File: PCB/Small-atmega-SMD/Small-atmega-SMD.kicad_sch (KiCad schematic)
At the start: 28 parts, among them J1 Daisy port out, J2 ICSP_ISP6, J3 UART, J4 Daisy port in, K1 HYC77-TF09-200, U1 PC817C-S, U2 ATmega328P-AU, U3 SE5218, U4 TXB0104PWR, Y1 Crystal_GND2

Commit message: More OCD
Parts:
- Y1: value Crystal_GND2 -> Resonator_GND2
- renumbered C5 to C2, C2 to C3, C3 to C4, C4 to C5
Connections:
- net RDDATA_in renamed RDDATA
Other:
- note added: "APPLE II INTERFACE"
- note added: "MICROSD CARD HOLDER"
- note added: "MICROSD LEVEL SHIFTER"
- note added: "MICROSD VOLTAGE REGULATOR"
- note added: "MINIMAL "ARDUINO NANO""
- note removed: "MICRO SD CARD HOLDER & CAPACITOR"
- note removed: "VOLTAGE LEVEL TRANSLATOR"
- note removed: "VOLTAGE REGULATOR"
- title: BurgerDisk PCB - Angled DB19 version -> Integrated Small BurgerDisk PCB
- moved on the sheet: C1, C2, C3, C4, C5, C6, C7, C8, D1, D2, D3, J1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

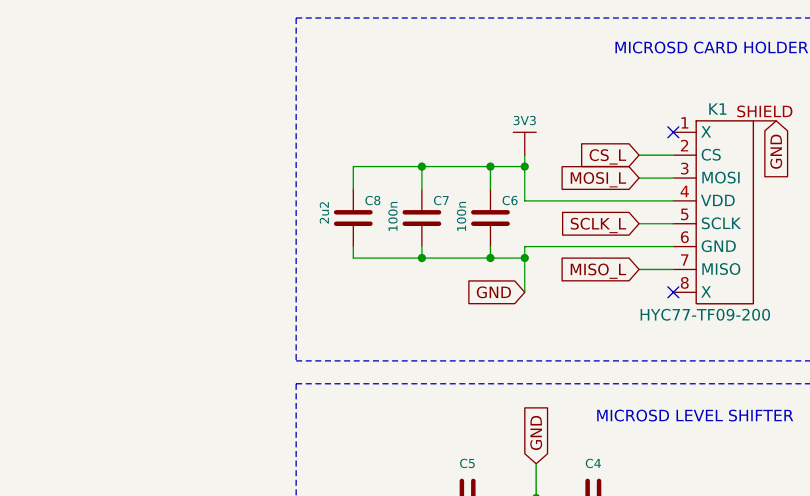
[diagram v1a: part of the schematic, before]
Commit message: Fix microSD caps
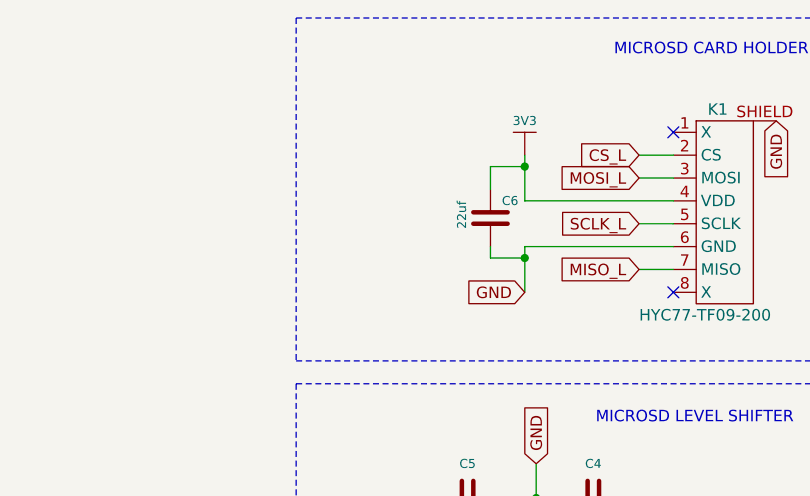
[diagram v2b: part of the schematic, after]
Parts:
- removed C7: 100n, Capacitor_SMD:C_0603_1608Metric, symbol e-radionica.com schematics:0603C
- removed C8: 2u2, Capacitor_SMD:C_0603_1608Metric, symbol e-radionica.com schematics:0603C
- C6: value 100n -> 22uf; footprint Capacitor_SMD:C_0603_1608Metric -> Capacitor_SMD:C_0805_2012Metric; LCSC C1590 -> C45783

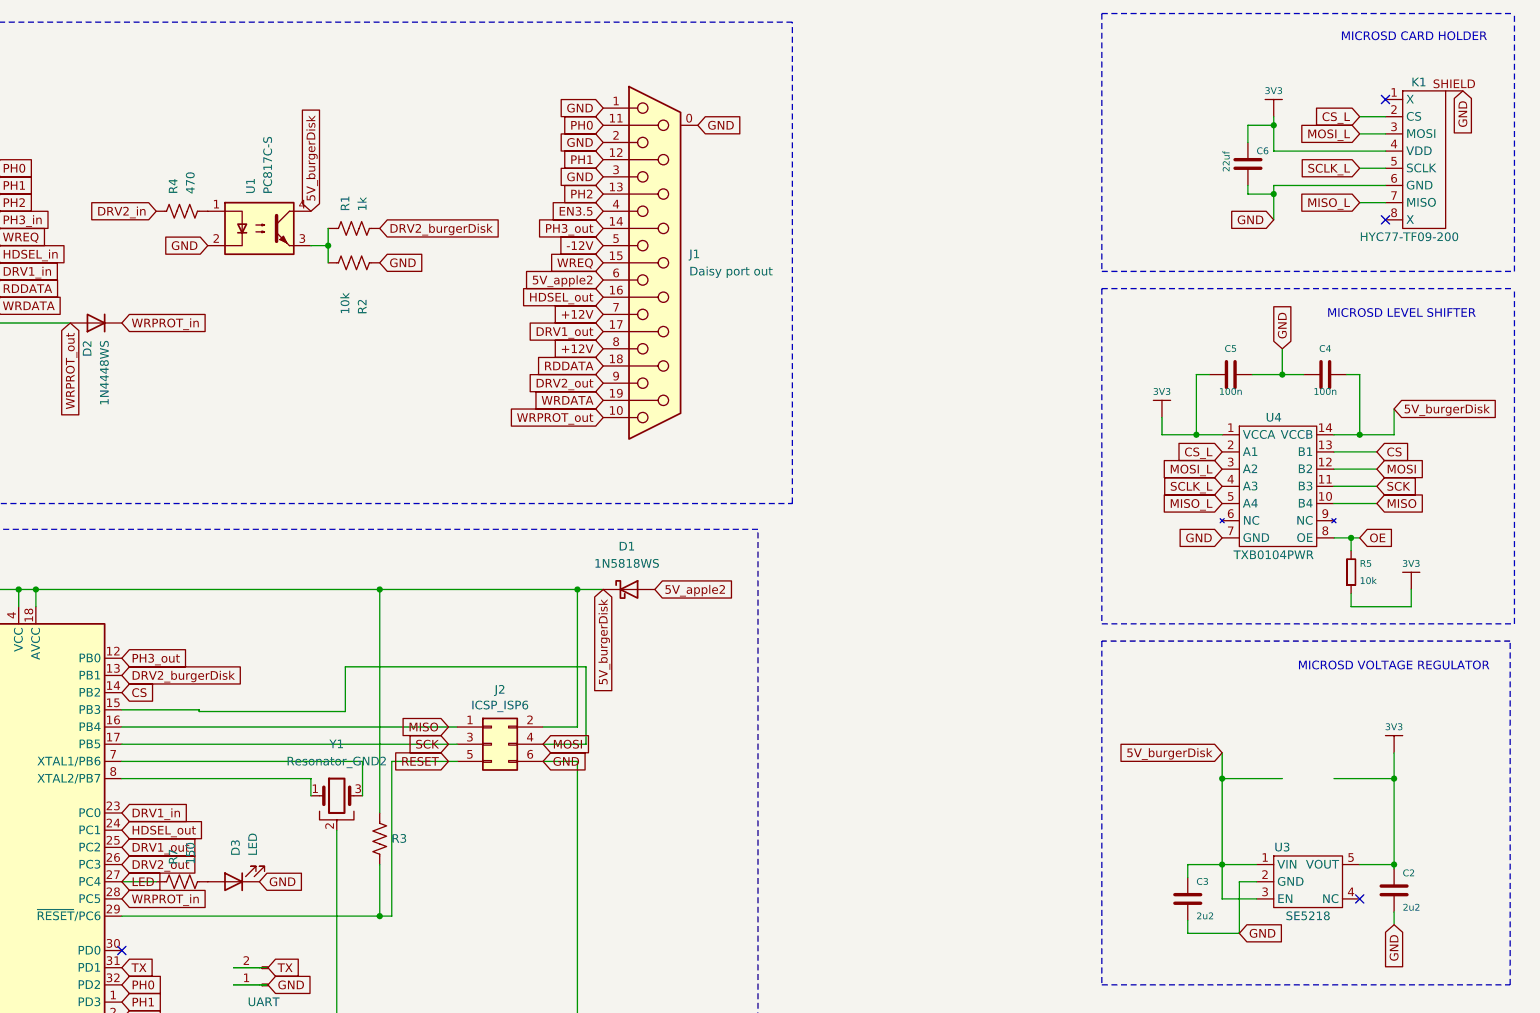
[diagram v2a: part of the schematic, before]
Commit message: Add SD module header, for hackers
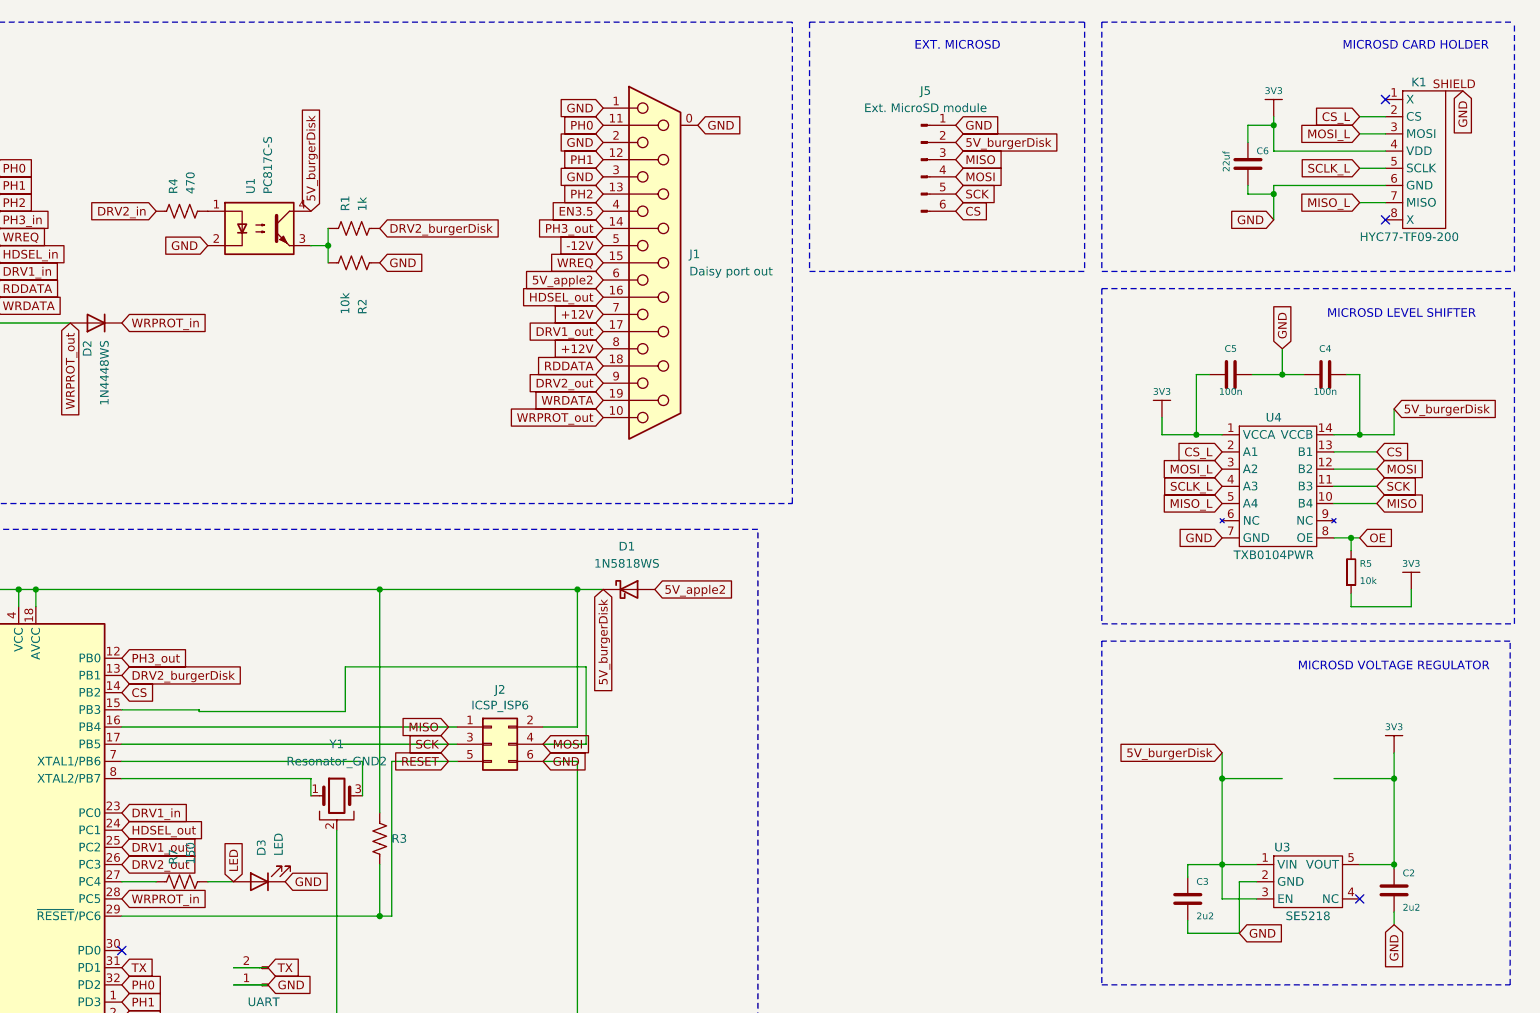
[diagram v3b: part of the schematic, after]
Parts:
- added J5: Ext. MicroSD module, Connector_PinHeader_2.54mm:PinHeader_1x06_P2.54mm_Vertical, symbol Connector:Conn_01x06_Pin
- C1: LCSC C28233 -> C1590
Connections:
- net 5V_burgerDisk: now also J5.2 (Pin_2)
- net CS: now also J5.6 (Pin_6)
- net GND: now also J5.1 (Pin_1)
- net LED: now also D3.2 (A), R7.1; no longer R7.2, U2.27 (PC4)
- net MISO: now also J5.3 (Pin_3)
- net MOSI: now also J5.4 (Pin_4)
- net SCK: now also J5.5 (Pin_5)
- new net: R7.2, U2.27 (PC4)
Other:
- note added: "EXT. MICROSD"
- moved on the sheet: D3

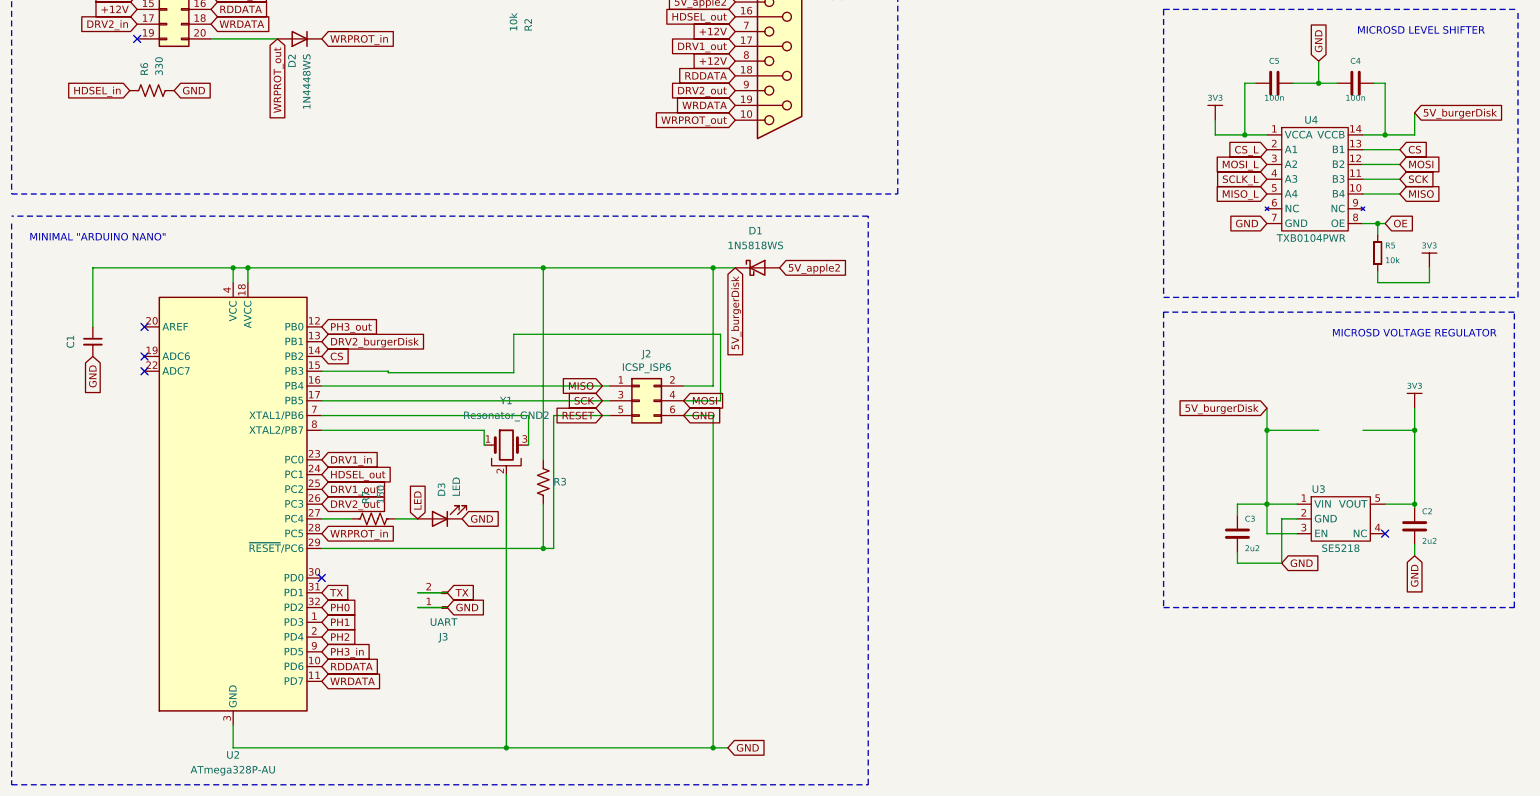
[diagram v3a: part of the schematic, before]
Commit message: Add solder pads for hacking
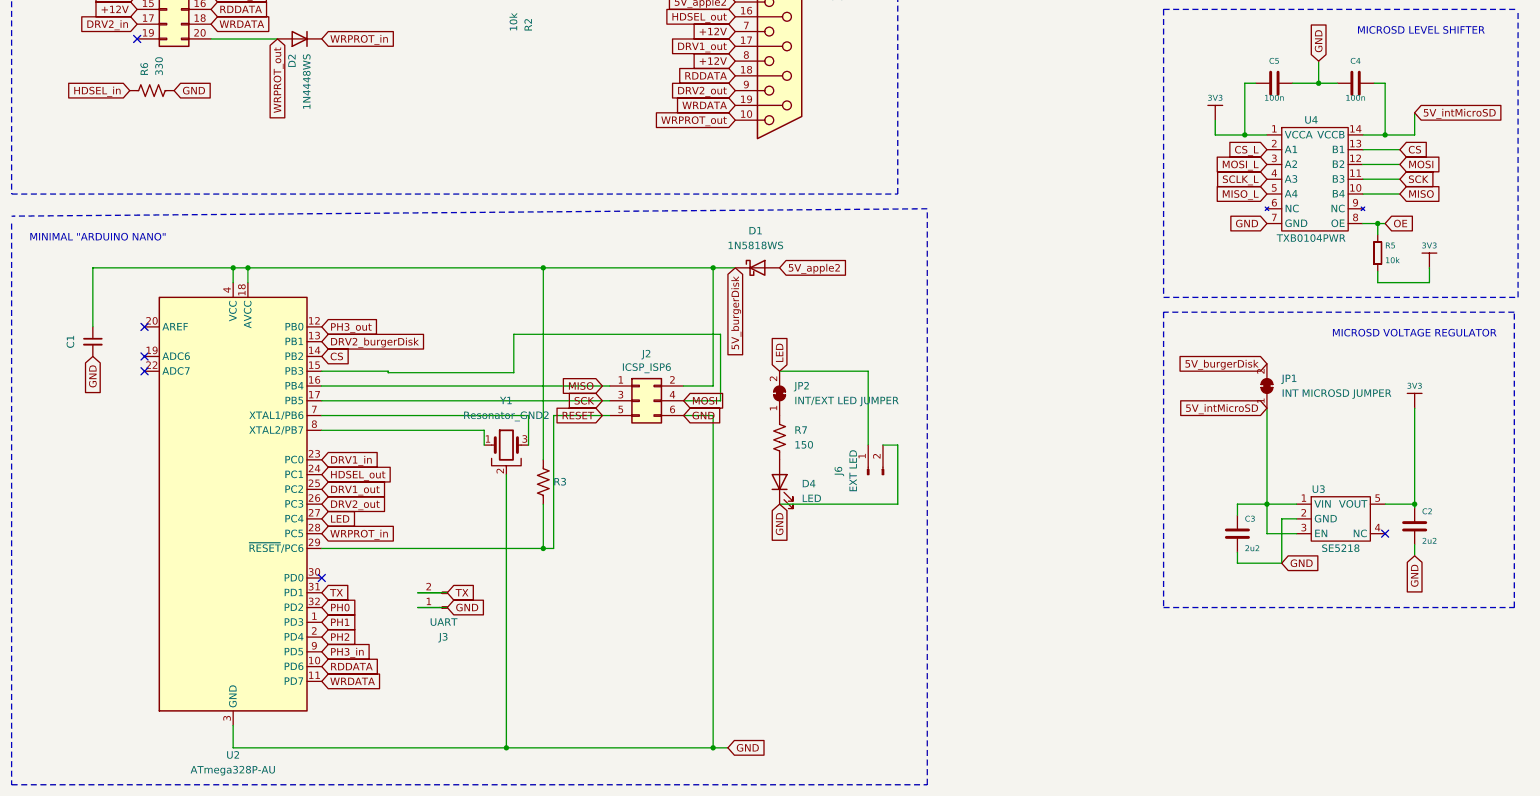
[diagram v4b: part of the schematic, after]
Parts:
- removed D3: LED, LED_THT:LED_D3.0mm, symbol Device:LED
- added D4: LED, LED_THT:LED_D3.0mm, symbol Device:LED
- added J6: EXT LED, Connector_PinHeader_2.54mm:PinHeader_1x02_P2.54mm_Vertical, symbol Connector:Conn_01x02_Pin
- added JP1: INT MICROSD JUMPER, Jumper:SolderJumper-2_P1.3mm_Bridged_Pad1.0x1.5mm, symbol Jumper:SolderJumper_2_Bridged
- added JP2: INT/EXT LED JUMPER, Jumper:SolderJumper-2_P1.3mm_Bridged_Pad1.0x1.5mm, symbol Jumper:SolderJumper_2_Bridged
- C1: value 100nF -> 100n
- J3: LCSC C6273326 -> C32713268
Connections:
- net 5V_burgerDisk: now also JP1.2 (B); no longer C3.2, C4.2, U3.1 (VIN), U3.3 (EN), U4.14 (VCCB)
- net GND: now also D4.1 (K), J6.2 (GND)
- net LED: now also U2.27 (PC4), J6.1 (+5V), JP2.2 (B); no longer R7.1
- net at R7.2: now also JP2.1 (A); no longer U2.27 (PC4)
- new net: D4.2 (A), R7.1
- new net 5V_intMicroSD: C3.2, C4.2, JP1.1 (A), U3.1 (VIN), U3.3 (EN), U4.14 (VCCB)
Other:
- moved on the sheet: R7

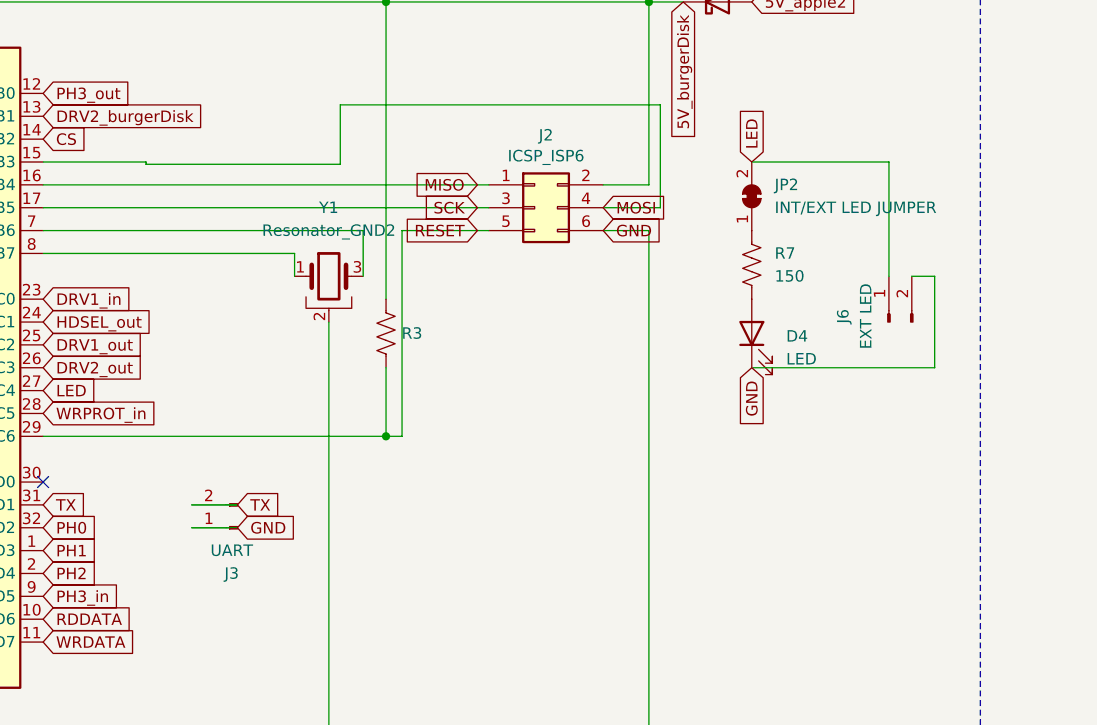
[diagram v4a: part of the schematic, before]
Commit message: Switch some parts to Basic
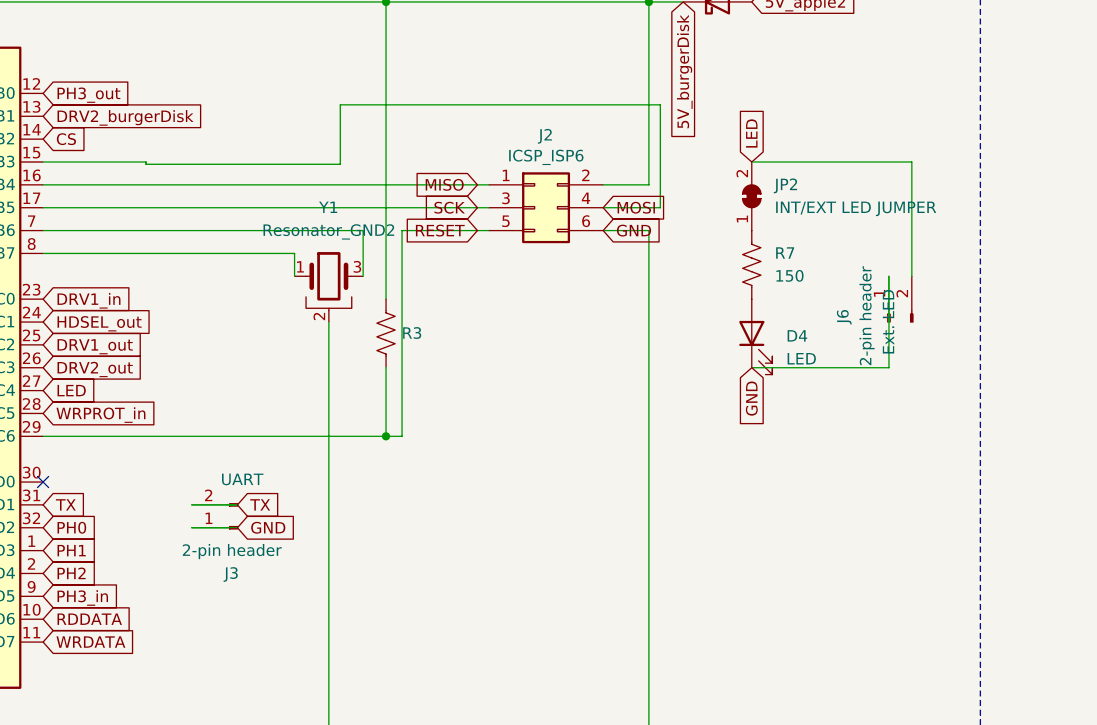
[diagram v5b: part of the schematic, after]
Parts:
- C1, C4, C5: LCSC C1590 -> C14663
- C2, C3: LCSC C1607 -> C23630
- J3: value UART -> 2-pin header
- J6: value EXT LED -> 2-pin header
- JP1, JP2: now left out of the parts list
- R1: LCSC C177343 -> C21190
- R2, R3, R5: LCSC C177337 -> C25804
- R6: LCSC C177341 -> C23138
- R7: LCSC C177290 -> C22808
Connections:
- net GND: now also J6.1 (+5V); no longer J6.2 (GND)
- net LED: now also J6.2 (GND); no longer J6.1 (+5V)
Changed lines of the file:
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@@
 		)
 	)
+	(wire
+		(pts
+			(xy 167.64 123.19) (xy 167.64 135.89)
+		)
+		(stroke
+			(width 0)
+			(type default)
+		)
+	)
 	(polyline
 		(pts
@@
 	(wire
 		(pts
-			(xy 165.1 123.19) (xy 165.1 135.89)
-		)
-		(stroke
-			(width 0)
-			(type default)
-		)
-	)
-	(wire
-		(pts
 			(xy 241.3 40.64) (xy 257.81 40.64)
 		)
@@
 	(wire
 		(pts
-			(xy 170.18 135.89) (xy 170.18 146.05)
+			(xy 241.3 45.72) (xy 257.81 45.72)
 		)
 		(stroke
 			(width 0)
-			(type default)
+			(type solid)
 		)
 	)
 	(wire
 		(pts
-			(xy 241.3 45.72) (xy 257.81 45.72)
+			(xy 165.1 146.05) (xy 165.1 135.89)
 		)
 		(stroke
 			(width 0)
-			(type solid)
+			(type default)
 		)
 	)
@@
 	(wire
 		(pts
+			(xy 149.86 146.05) (xy 165.1 146.05)
+		)
+		(stroke
+			(width 0)
+			(type default)
+		)
+	)
+	(wire
+		(pts
 			(xy 242.57 73.66) (xy 245.745 73.66)
 		)
@@
 		)
 	)
-	(wire
-		(pts
-			(xy 170.18 146.05) (xy 149.86 146.05)
-		)
-		(stroke
-			(width 0)
-			(type default)
-		)
-	)
 	(polyline
 		(pts
@@
 	(wire
 		(pts
-			(xy 149.86 123.19) (xy 165.1 123.19)
+			(xy 149.86 123.19) (xy 167.64 123.19)
 		)
 		(stroke
@@
 	(wire
 		(pts
-			(xy 167.64 135.89) (xy 170.18 135.89)
-		)
-		(stroke
-			(width 0)
-			(type default)
-		)
-	)
-	(wire
-		(pts
 			(xy 82.55 123.444) (xy 82.55 123.19)
 		)
@@
 			)
 		)
-		(property "LCSC" "C1590"
+		(property "LCSC" "C14663"
 			(at 234.95 73.66 0)
 			(effects
@@
 			)
 		)
-		(property "LCSC" "C1590"
+		(property "LCSC" "C14663"
 			(at 31.75 118.11 90)
 			(effects
@@
 			)
 		)
-		(property "Value" "UART"
+		(property "Value" "2-pin header"
 			(at 92.075 166.37 0)
 			(effects
@@
 			)
 		)
-		(property "Description" ""
-			(at 92.71 163.83 0)
+		(property "Description" "UART"
+			(at 93.218 158.496 0)
 			(effects
 				(font
@@
 			)
 		)
-		(property "LCSC" "C177337"
+		(property "LCSC" "C25804"
 			(at 105.41 57.15 0)
 			(effects
@@
 			)
 		)
-		(property "LCSC" "C1607"
+		(property "LCSC" "C23630"
 			(at 259.08 149.86 90)
 			(effects
@@
 		(unit 1)
 		(exclude_from_sim no)
-		(in_bom yes)
+		(in_bom no)
 		(on_board yes)
 		(dnp no)
@@
 			)
 		)
-		(property "Value" "EXT LED"
+		(property "Value" "2-pin header"
 			(at 162.56 140.335 0)
 			(effects
@@
 			)
 		)
-		(property "Description" ""
+		(property "Description" "Ext. LED"
 			(at 165.1 140.97 0)
 			(effects
@@
 			)
 		)
-		(property "LCSC" "C177337"
+		(property "LCSC" "C25804"
 			(at 252.73 102.87 90)
 			(effects
@@
 			)
 		)
-		(property "LCSC" "C177337"
+		(property "LCSC" "C25804"
 			(at 109.22 142.24 0)
 			(effects
@@
 		(unit 1)
 		(exclude_from_sim no)
-		(in_bom yes)
+		(in_bom no)
 		(on_board yes)
 		(dnp no)
@@
 			)
 		)
-		(property "LCSC" "C177290"
+		(property "LCSC" "C22808"
 			(at 149.86 134.62 0)
 			(effects
@@
 			)
 		)
-		(property "LCSC" "C1607"
+		(property "LCSC" "C23630"
 			(at 228.6 151.13 90)
 			(effects
@@
 			)
 		)
-		(property "LCSC" "C177341"
+		(property "LCSC" "C23138"
 			(at 41.91 74.93 0)
 			(effects
@@
 			)
 		)
-		(property "LCSC" "C1590"
+		(property "LCSC" "C14663"
 			(at 248.92 73.66 0)
 			(effects
@@
 			)
 		)
-		(property "LCSC" "C177343"
+		(property "LCSC" "C21190"
 			(at 105.41 52.07 0)
 			(effects
